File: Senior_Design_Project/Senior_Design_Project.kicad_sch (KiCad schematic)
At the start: 16 parts, among them J1 Conn_01x02_Female, J2 SMA_Connector, U1 STM32F030C6Tx, U2 DAC08, U3 ADC, U4 Mixer, U5 Mixer, X1 VCO, X2 VCO

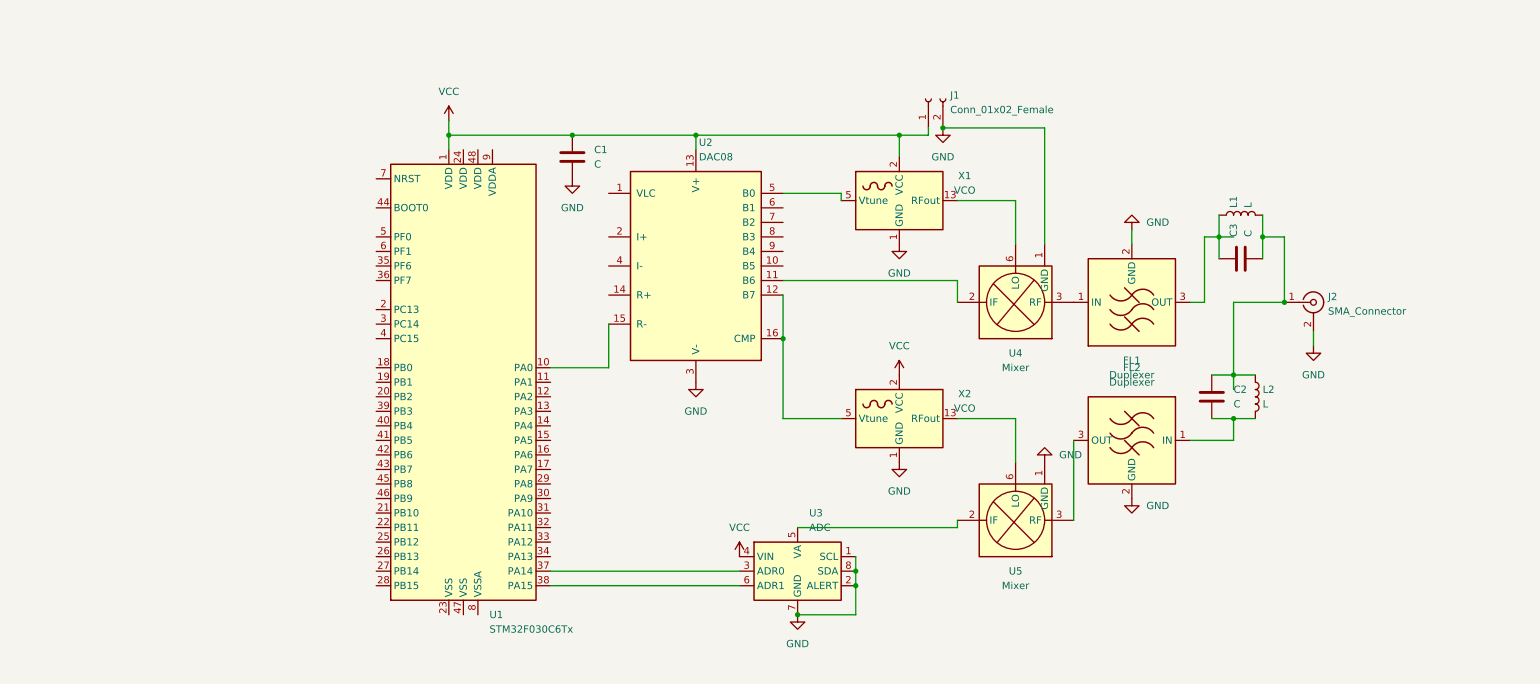
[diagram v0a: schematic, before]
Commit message: antenna matching netowrks for Rx and Tx added partially
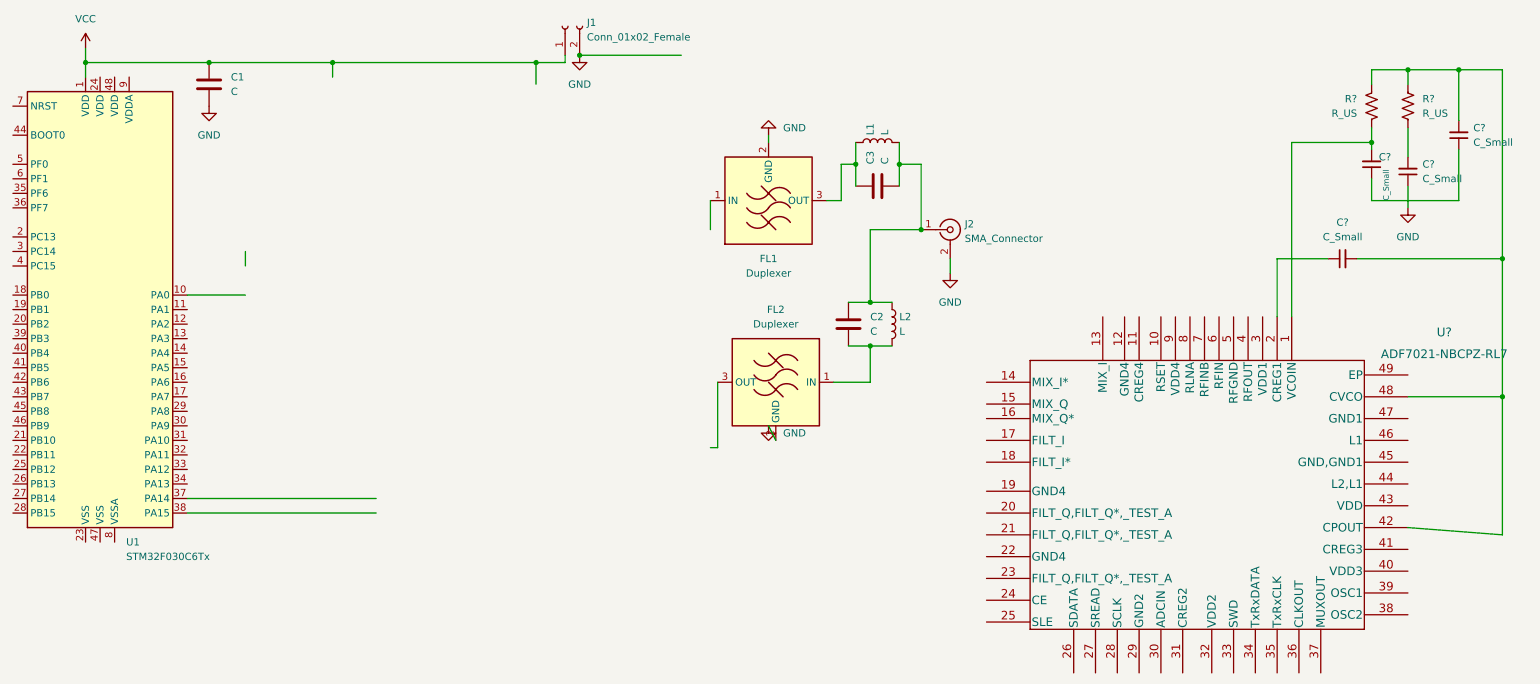
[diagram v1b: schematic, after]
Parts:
- removed U2: DAC08, Package_SO:SOIC-16_4.55x10.3mm_P1.27mm, symbol Analog_DAC:DAC08
- removed U3: ADC, Package_SO:MSOP-8_3x3mm_P0.65mm, symbol Analog_ADC:ADC081C021CIMM
- removed U4, U5: Mixer, RF_Mini-Circuits:Mini-Circuits_CD542_LandPatternPL-052, symbol RF_Mixer:ADEX-10
- removed X1, X2: VCO, RF_Mini-Circuits:Mini-Circuits_BK377_LandPatternPL-005, symbol Oscillator:JTOS-25
- added C? (x4): C_Small, symbol Device:C_Small
- added R? (x2): R_US, symbol Device:R_US
- added U?: ADF7021-NBCPZ-RL7, ADF7021:QFN50P700X700X80-49N, symbol 2023-01-05_17-34-24:ADF7021-NBCPZ-RL7
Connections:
- net GND: now also C?.1
- new net: C?.2, R?.1
- new net: C?.2, C?.2, R?.2, R?.2, U?.42 (CPOUT), U?.48 (CVCO)
- new net: C?.2, R?.1, U?.1 (VCOIN)
- new net: C?.1, U?.2 (CREG1)
- new net: C?.1, C?.1
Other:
- moved on the sheet: C1, C2, C3, FL1, FL2, J1, J2, L1, L2, U1
